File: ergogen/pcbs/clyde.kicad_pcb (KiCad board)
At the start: 2 copper layers, 100 x 85.7 mm, 23 parts, among them U0 Pico

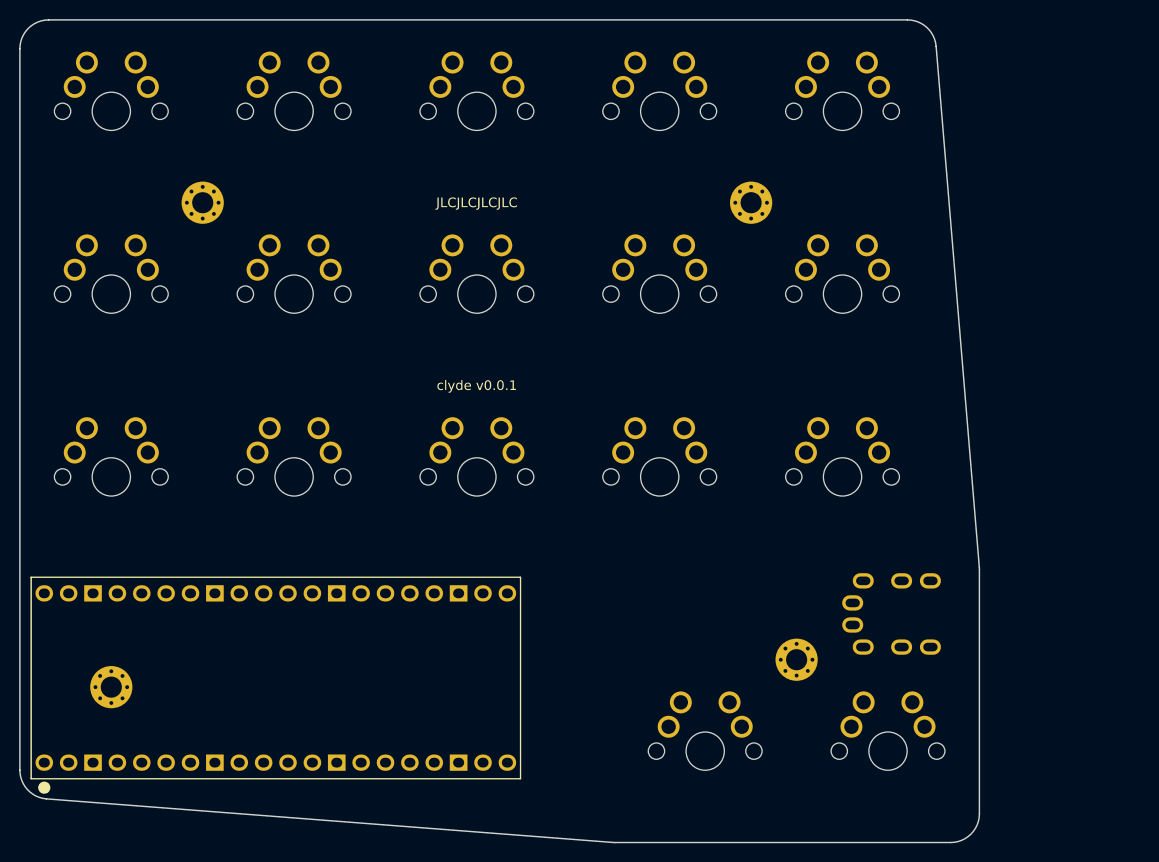
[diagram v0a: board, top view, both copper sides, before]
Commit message: 36 key version
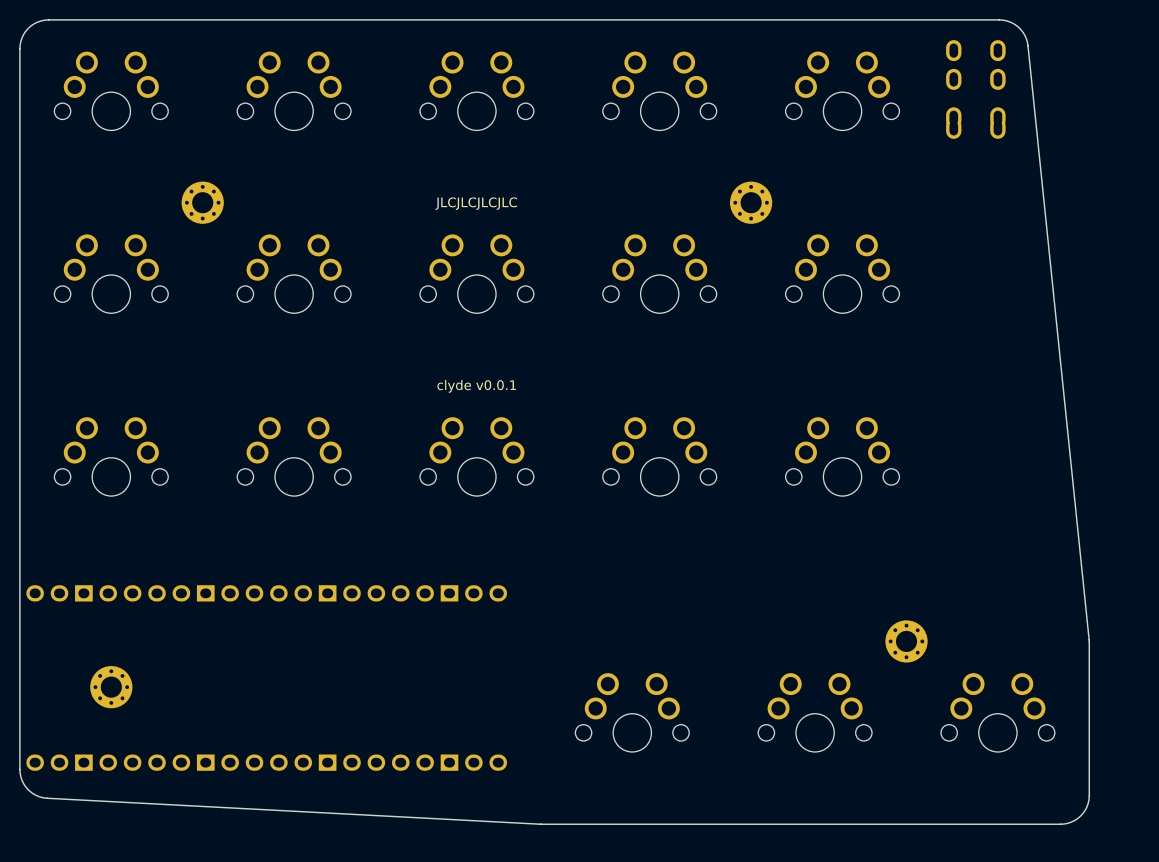
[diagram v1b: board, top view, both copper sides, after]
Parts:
- added S18: , MX, F.Cu at (244.8, 179.1)
- U0: value Pico -> (none); footprint RPi_Pico_TH_oval_face_up -> RPi_Pico_TH_oval_face_down
- moved TRRS1 63.2 mm to (244.8, 104.8), turned to 0 degrees
- moved _4 11.6 mm to (235.3, 169.5)
- moved S16 7.83 mm to (206.7, 179.1)
- moved S17 7.83 mm to (225.7, 179.1)
- moved U0 0.95 mm to (168.6, 173.4)
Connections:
- S17 pad 1: thumbfan_far_home -> thumbfan_home_home
- TRRS1 pad 1: VSYS -> GND
- TRRS1 pad 3: GP9 -> VSYS
- TRRS1 pad 4: GP8 -> GP12
- U0 pad 1: GP0 -> matrix_pinky_top
- U0 pad 10: GP7 -> matrix_middle_home
- U0 pad 11: GP8 -> matrix_middle_bottom
- U0 pad 12: GP9 -> matrix_index_top
- U0 pad 14: GP10 -> matrix_index_home
- U0 pad 15: thumbfan_far_home -> matrix_index_bottom
- U0 pad 16: thumbfan_near_home -> GP12
- U0 pad 17: matrix_inner_top -> matrix_inner_bottom
- U0 pad 2: GP1 -> matrix_pinky_home
- U0 pad 20: matrix_inner_bottom -> matrix_inner_top
- U0 pad 21: matrix_index_bottom -> thumbfan_far_home
- U0 pad 22: matrix_index_home -> thumbfan_home_home
- U0 pad 24: matrix_index_top -> thumbfan_near_home
- U0 pad 25: matrix_middle_bottom -> GP19
- U0 pad 26: matrix_middle_home -> GP20
- U0 pad 27: matrix_middle_top -> GP21
- U0 pad 29: matrix_ring_top -> GP22
- U0 pad 30: matrix_ring_home -> GP26
- U0 pad 31: matrix_ring_bottom -> GP27
- U0 pad 32: matrix_pinky_bottom -> GP28
- U0 pad 34: matrix_pinky_home -> GP29
- U0 pad 36: matrix_pinky_top -> GP24
- U0 pad 4: GP2 -> matrix_pinky_bottom
- U0 pad 5: GP3 -> matrix_ring_bottom
- U0 pad 6: GP4 -> matrix_ring_home
- U0 pad 7: GP5 -> matrix_ring_top
- U0 pad 9: GP6 -> matrix_middle_top
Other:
- board size 100 x 85.7 mm -> 111.4 x 83.8 mm

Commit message: hatch groundfill; star silkscreen
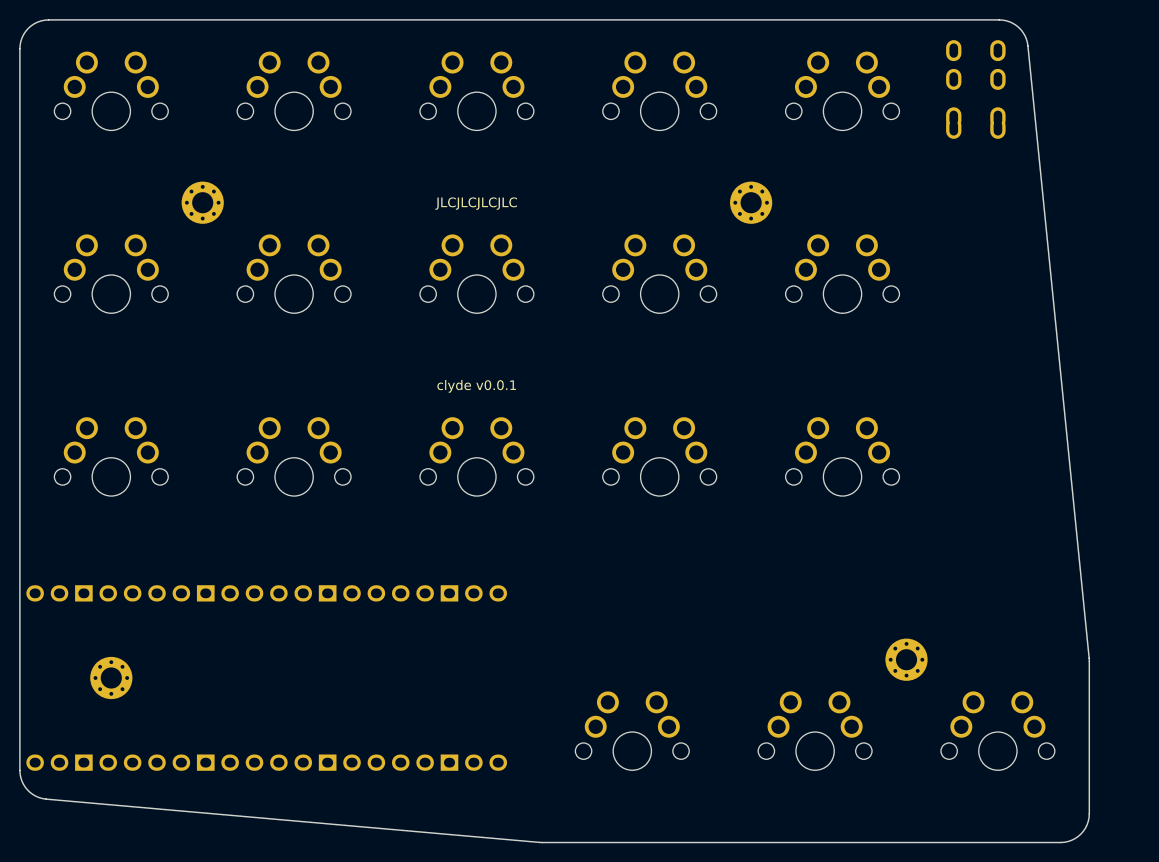
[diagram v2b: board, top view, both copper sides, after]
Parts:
- moved S16 1.91 mm to (206.7, 181.0)
- moved S17 1.91 mm to (225.7, 181.0)
- moved S18 1.91 mm to (244.8, 181.0)
- moved _4 1.91 mm to (235.3, 171.4)
- moved _5 0.95 mm to (152.4, 173.4)
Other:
- board size 111.4 x 83.8 mm -> 111.4 x 85.7 mm
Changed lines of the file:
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@@
           )
       (module MX (layer F.Cu)
-      (at 206.69250000000002 179.07 0)
+      (at 206.69250000000002 180.975 0)
       (fp_text reference "S16" (at 0 0) (layer F.SilkS) hide (effects (font (size 1.27 1.27) (thickness 0.15))))
       (fp_text value "" (at 0 0) (layer F.SilkS) hide (effects (font (size 1.27 1.27) (thickness 0.15))))
@@
           )
       (module MX (layer F.Cu)
-      (at 225.74250000000004 179.07 0)
+      (at 225.74250000000004 180.975 0)
       (fp_text reference "S17" (at 0 0) (layer F.SilkS) hide (effects (font (size 1.27 1.27) (thickness 0.15))))
       (fp_text value "" (at 0 0) (layer F.SilkS) hide (effects (font (size 1.27 1.27) (thickness 0.15))))
@@
           )
       (module MX (layer F.Cu)
-      (at 244.79250000000002 179.07 0)
+      (at 244.79250000000002 180.975 0)
       (fp_text reference "S18" (at 0 0) (layer F.SilkS) hide (effects (font (size 1.27 1.27) (thickness 0.15))))
       (fp_text value "" (at 0 0) (layer F.SilkS) hide (effects (font (size 1.27 1.27) (thickness 0.15))))
@@
             )
     (module "MountingHole_2.2mm_M2_Pad_Via" (version 20210722) (generator pcbnew) (layer "F.Cu")
-      (at 235.26750000000004 169.545 0)
+      (at 235.26750000000004 171.45 0)
       (fp_text reference "_4" (at 0 -3.2) (layer "F.SilkS") hide
         (effects (font (size 1 1) (thickness 0.15)))
@@
     )
     (module "MountingHole_2.2mm_M2_Pad_Via" (version 20210722) (generator pcbnew) (layer "F.Cu")
-      (at 152.4 174.3075 0)
+      (at 152.4 173.35500000000002 0)
       (fp_text reference "_5" (at 0 -3.2) (layer "F.SilkS") hide
         (effects (font (size 1 1) (thickness 0.15)))
@@
       (pad "1" thru_hole circle locked (at 0 -1.65) (size 0.7 0.7) (drill 0.4) (layers *.Cu *.Mask))
     )
-            (gr_line (start 142.875 182.89124247368423) (end 142.875 107.77499999999999) (angle 90) (layer Edge.Cuts) (width 0.15))
-(gr_line (start 145.875 104.77499999999999) (end 244.94297008970588 104.77499999999999) (angle 90) (layer Edge.Cuts) (width 0.15))
-(gr_line (start 247.92719999989208 107.46779999895125) (end 254.30172991018622 169.3918048418086) (angle 90) (layer Edge.Cuts) (width 0.15))
-(gr_line (start 254.31750000000002 169.699004842857) (end 254.31750000000002 185.595) (angle 90) (layer Edge.Cuts) (width 0.15))
-(gr_line (start 251.31750000000002 188.595) (end 197.246393 188.595) (angle 90) (layer Edge.Cuts) (width 0.15))
-(gr_line (start 197.08871659447507 188.59085350497236) (end 145.71732359447512 185.8870959786566) (angle 90) (layer Edge.Cuts) (width 0.15))
+            (gr_line (start 142.875 182.9891379754386) (end 142.875 107.77499999999999) (angle 90) (layer Edge.Cuts) (width 0.15))
+(gr_line (start 145.875 104.77499999999999) (end 244.93503728000002 104.77499999999999) (angle 90) (layer Edge.Cuts) (width 0.15))
+(gr_line (start 247.92014888990101 107.47648889901029) (end 254.30261160990108 171.30111609901041) (angle 90) (layer Edge.Cuts) (width 0.15))
+(gr_line (start 254.31750000000002 171.5996272000002) (end 254.31750000000002 187.5) (angle 90) (layer Edge.Cuts) (width 0.15))
+(gr_line (start 251.31750000000002 190.5) (end 197.29882707999988 190.5) (angle 90) (layer Edge.Cuts) (width 0.15))
+(gr_line (start 197.03667597053135 190.48852420794134) (end 145.61284889053147 185.97766218337998) (angle 90) (layer Edge.Cuts) (width 0.15))
 (gr_arc (start 145.875 107.77499999999999) (end 145.875 104.77499999999999) (angle -90) (layer Edge.Cuts) (width 0.15))
-(gr_arc (start 244.94297008970588 107.77499999999999) (end 247.92719998970588 107.4678) (angle -84.1226099916367) (layer Edge.Cuts) (width 0.15))
-(gr_arc (start 251.31750000000002 169.699004842857) (end 254.31750000000002 169.699004842857) (angle -5.877390008356565) (layer Edge.Cuts) (width 0.15))
-(gr_arc (start 251.31750000000002 185.595) (end 251.31750000000002 188.595) (angle -90) (layer Edge.Cuts) (width 0.15))
-(gr_arc (start 197.246393 185.595) (end 197.0887166 188.5908535) (angle -3.0127856973452367) (layer Edge.Cuts) (width 0.15))
-(gr_arc (start 145.875 182.89124247368423) (end 142.875 182.89124247368423) (angle -86.98721430265584) (layer Edge.Cuts) (width 0.15))
+(gr_arc (start 244.93503728000002 107.77499999999999) (end 247.92014888000003 107.47648889999999) (angle -84.28940800273658) (layer Edge.Cuts) (width 0.15))
+(gr_arc (start 251.31750000000002 171.5996272000002) (end 254.31750000000002 171.5996272000002) (angle -5.710591997265208) (layer Edge.Cuts) (width 0.15))
+(gr_arc (start 251.31750000000002 187.5) (end 251.31750000000002 190.5) (angle -90) (layer Edge.Cuts) (width 0.15))
+(gr_arc (start 197.29882707999988 187.5) (end 197.03667597999987 190.4885242) (angle -5.013111151541295) (layer Edge.Cuts) (width 0.15))
+(gr_arc (start 145.875 182.9891379754386) (end 142.875 182.9891379754386) (angle -84.9868888484587) (layer Edge.Cuts) (width 0.15))
 )

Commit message: stagger thumb cluster
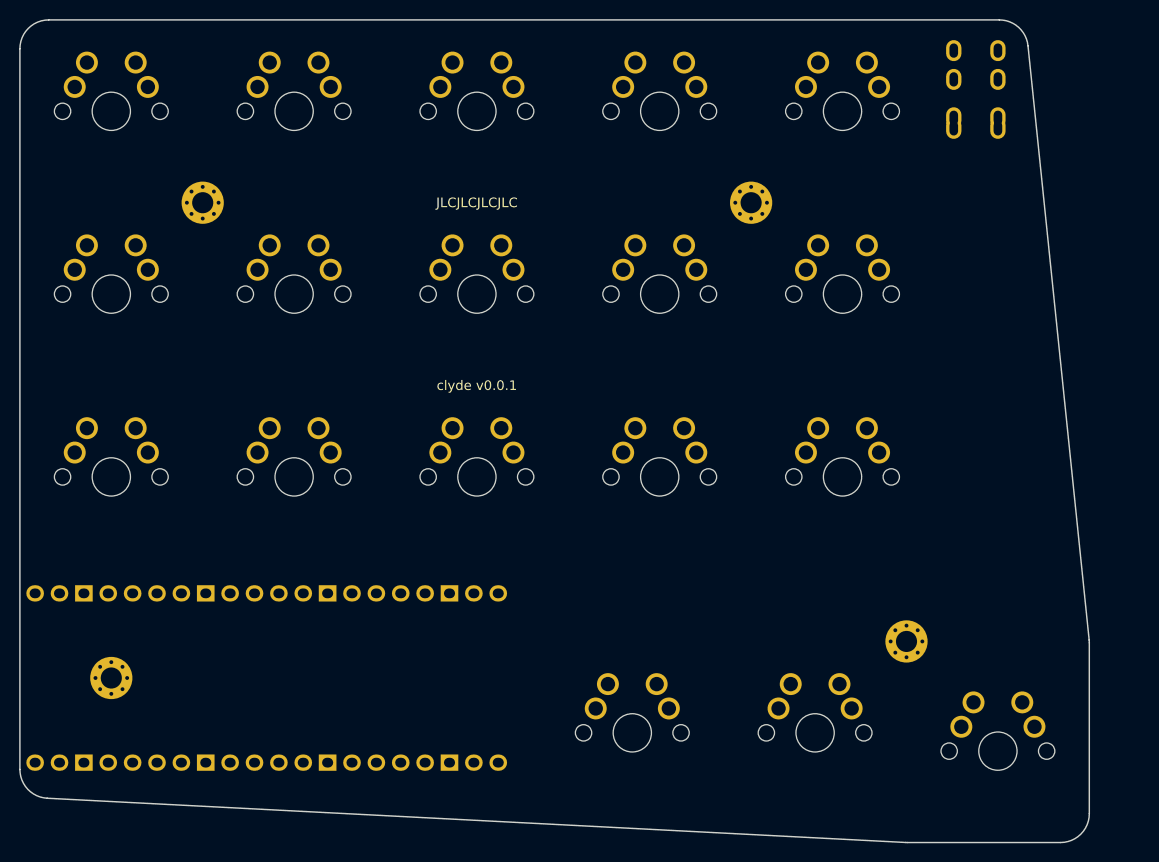
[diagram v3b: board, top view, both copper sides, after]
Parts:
- moved S16 1.91 mm to (206.7, 179.1)
- moved S17 1.91 mm to (225.7, 179.1)
- moved _4 1.91 mm to (235.3, 169.5)
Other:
- outline, holes or cut-outs redrawn
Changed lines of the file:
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@@
           )
       (module MX (layer F.Cu)
-      (at 206.69250000000002 180.975 0)
+      (at 206.69250000000002 179.07 0)
       (fp_text reference "S16" (at 0 0) (layer F.SilkS) hide (effects (font (size 1.27 1.27) (thickness 0.15))))
       (fp_text value "" (at 0 0) (layer F.SilkS) hide (effects (font (size 1.27 1.27) (thickness 0.15))))
@@
           )
       (module MX (layer F.Cu)
-      (at 225.74250000000004 180.975 0)
+      (at 225.74250000000004 179.07 0)
       (fp_text reference "S17" (at 0 0) (layer F.SilkS) hide (effects (font (size 1.27 1.27) (thickness 0.15))))
       (fp_text value "" (at 0 0) (layer F.SilkS) hide (effects (font (size 1.27 1.27) (thickness 0.15))))
@@
             )
     (module "MountingHole_2.2mm_M2_Pad_Via" (version 20210722) (generator pcbnew) (layer "F.Cu")
-      (at 235.26750000000004 171.45 0)
+      (at 235.26750000000004 169.545 0)
       (fp_text reference "_4" (at 0 -3.2) (layer "F.SilkS") hide
         (effects (font (size 1 1) (thickness 0.15)))
@@
       (pad "1" thru_hole circle locked (at 0 -1.65) (size 0.7 0.7) (drill 0.4) (layers *.Cu *.Mask))
     )
-            (gr_line (start 142.875 182.9891379754386) (end 142.875 107.77499999999999) (angle 90) (layer Edge.Cuts) (width 0.15))
-(gr_line (start 145.875 104.77499999999999) (end 244.93503728000002 104.77499999999999) (angle 90) (layer Edge.Cuts) (width 0.15))
-(gr_line (start 247.92014888990101 107.47648889901029) (end 254.30261160990108 171.30111609901041) (angle 90) (layer Edge.Cuts) (width 0.15))
-(gr_line (start 254.31750000000002 171.5996272000002) (end 254.31750000000002 187.5) (angle 90) (layer Edge.Cuts) (width 0.15))
-(gr_line (start 251.31750000000002 190.5) (end 197.29882707999988 190.5) (angle 90) (layer Edge.Cuts) (width 0.15))
-(gr_line (start 197.03667597053135 190.48852420794134) (end 145.61284889053147 185.97766218337998) (angle 90) (layer Edge.Cuts) (width 0.15))
+            (gr_line (start 142.875 182.88815625463917) (end 142.875 107.77499999999999) (angle 90) (layer Edge.Cuts) (width 0.15))
+(gr_line (start 145.875 104.77499999999999) (end 244.94297008970588 104.77499999999999) (angle 90) (layer Edge.Cuts) (width 0.15))
+(gr_line (start 247.92719999989208 107.46779999895125) (end 254.30172991018622 169.3918048418086) (angle 90) (layer Edge.Cuts) (width 0.15))
+(gr_line (start 254.31750000000002 169.699004842857) (end 254.31750000000002 187.5) (angle 90) (layer Edge.Cuts) (width 0.15))
+(gr_line (start 251.31750000000002 190.5) (end 235.34476865999997 190.5) (angle 90) (layer Edge.Cuts) (width 0.15))
+(gr_line (start 235.19033465459398 190.49602240487596) (end 145.720565994594 185.8841786595152) (angle 90) (layer Edge.Cuts) (width 0.15))
 (gr_arc (start 145.875 107.77499999999999) (end 145.875 104.77499999999999) (angle -90) (layer Edge.Cuts) (width 0.15))
-(gr_arc (start 244.93503728000002 107.77499999999999) (end 247.92014888000003 107.47648889999999) (angle -84.28940800273658) (layer Edge.Cuts) (width 0.15))
-(gr_arc (start 251.31750000000002 171.5996272000002) (end 254.31750000000002 171.5996272000002) (angle -5.710591997265208) (layer Edge.Cuts) (width 0.15))
+(gr_arc (start 244.94297008970588 107.77499999999999) (end 247.92719998970588 107.4678) (angle -84.1226099916367) (layer Edge.Cuts) (width 0.15))
+(gr_arc (start 251.31750000000002 169.699004842857) (end 254.31750000000002 169.699004842857) (angle -5.877390008356565) (layer Edge.Cuts) (width 0.15))
 (gr_arc (start 251.31750000000002 187.5) (end 251.31750000000002 190.5) (angle -90) (layer Edge.Cuts) (width 0.15))
-(gr_arc (start 197.29882707999988 187.5) (end 197.03667597999987 190.4885242) (angle -5.013111151541295) (layer Edge.Cuts) (width 0.15))
-(gr_arc (start 145.875 182.9891379754386) (end 142.875 182.9891379754386) (angle -84.9868888484587) (layer Edge.Cuts) (width 0.15))
+(gr_arc (start 235.34476865999997 187.5) (end 235.19033465999996 190.4960224) (angle -2.9507764544792394) (layer Edge.Cuts) (width 0.15))
+(gr_arc (start 145.875 182.88815625463917) (end 142.875 182.88815625463917) (angle -87.04922354552087) (layer Edge.Cuts) (width 0.15))
 )
